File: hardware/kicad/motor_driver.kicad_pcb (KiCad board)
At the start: 2 copper layers, 50.5 x 39.8 mm, 17 parts, among them J1 Conn_01x05_Pin, J2 TO_MOTOR, J3 5V_IN, J4 PRT-10811, U1 ULN2003A

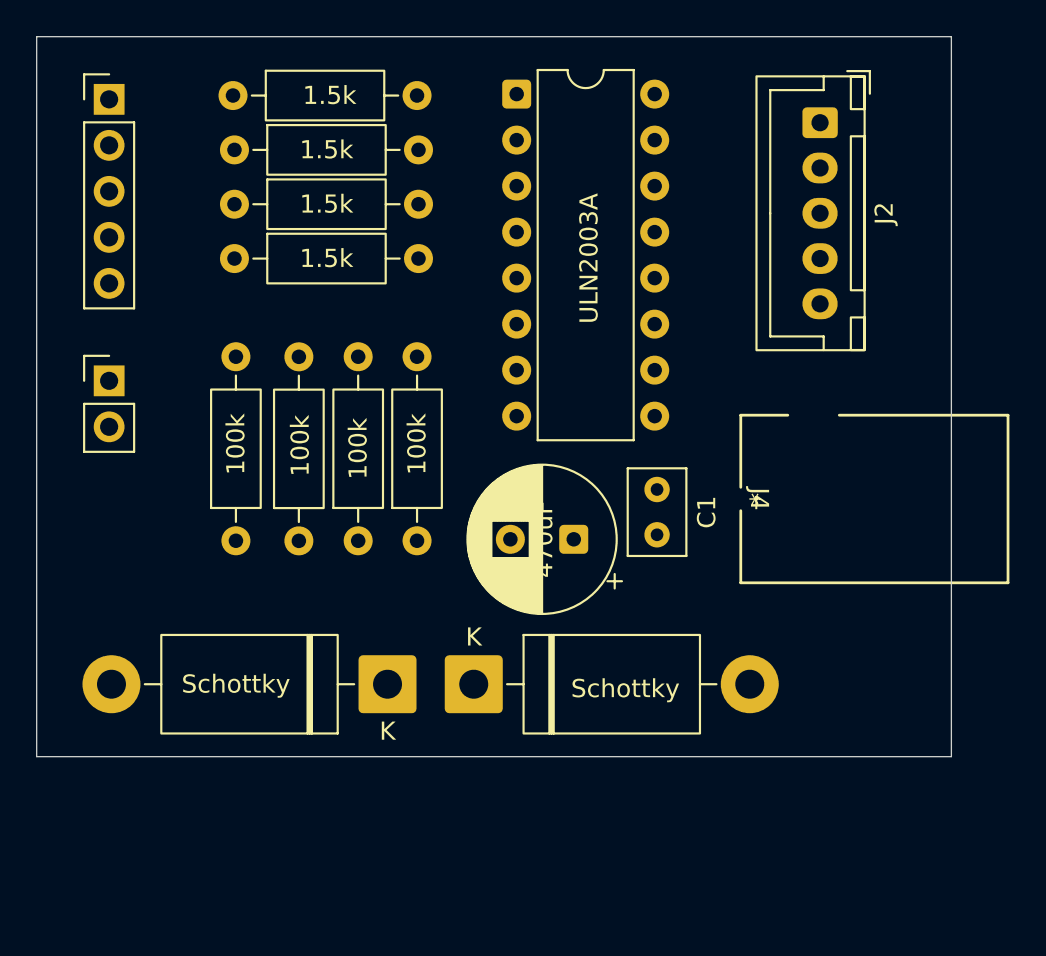
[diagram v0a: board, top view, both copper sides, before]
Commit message: perf: routed the components - PCB
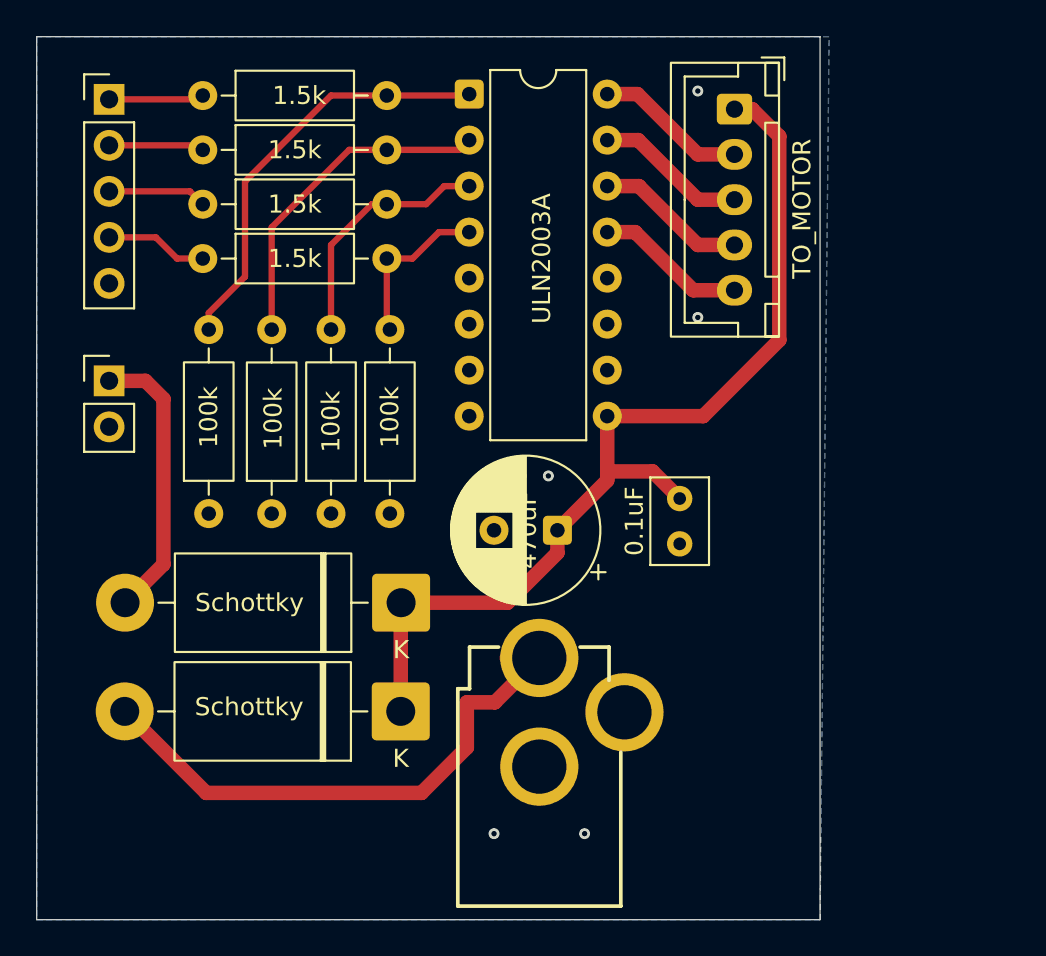
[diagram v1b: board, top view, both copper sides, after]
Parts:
- J4: value PRT-10811 -> Barrel_Jack_PTH; footprint Power Jack:PRT-10811_SPK -> PCM_SparkFun-Connector:Barrel_Jack_PTH
- moved J4 25.5 mm to (97.5, 72.5), turned to 0 degrees
- moved J2 4.78 mm to (108.3, 28.5)
- moved D2 4.56 mm to (89.9, 55.8)
- moved D1 4.30 mm to (89.8, 61.8), turned to 180 degrees
- moved U1 2.62 mm to (93.6, 27.7)
- moved R5 2.12 mm to (89.2, 50.8)
- moved R6 2.12 mm to (86.0, 50.8)
- moved R7 2.12 mm to (82.7, 50.8)
- moved R8 2.12 mm to (79.2, 50.8)
- moved R2 1.75 mm to (78.9, 30.8)
- moved R3 1.75 mm to (78.9, 33.8)
- moved R4 1.75 mm to (78.9, 36.8)
- moved R1 1.67 mm to (78.9, 27.8)
- moved 0.1uF 1.35 mm to (105.2, 50.0)
- moved C2 1.03 mm to (98.5, 51.8)
- renumbered C1 to 0.1uF
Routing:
- net /+5V_COM: track 0.00 -> 54.7 mm
- net Net-(D1-A): track 0.00 -> 31.1 mm
- net Net-(U1-I1): track 0.00 -> 23.4 mm
- net Net-(U1-I2): track 0.00 -> 18.5 mm
- net Net-(D2-A): track 0.00 -> 16.9 mm
- net Net-(U1-I3): track 0.00 -> 13.6 mm
- net Net-(U1-I4): track 0.00 -> 9.15 mm
- net Net-(J2-Pin_2): track 0.00 -> 8.40 mm
- net Net-(J2-Pin_3): track 0.00 -> 8.39 mm
- net Net-(J2-Pin_4): track 0.00 -> 8.37 mm
- net Net-(J2-Pin_5): track 0.00 -> 8.35 mm
- net /IN4: track 0.00 -> 5.65 mm
- net /IN3: track 0.00 -> 5.46 mm
- net /IN2: track 0.00 -> 5.27 mm
- net /IN1: track 0.00 -> 5.26 mm
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- added copper zone on B.Cu, net /GND
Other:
- board size 50.5 x 39.8 mm -> 43.2 x 48.8 mm
- board text added: "K"
